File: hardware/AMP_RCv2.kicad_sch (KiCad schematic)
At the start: 46 parts, among them J1 USB_C_Receptacle_USB2.0_16P, SW1 SW_UP, SW2 SW_LEFT, SW3 SW_DOWN, SW4 SW_RIGHT, SW5 ON/OFF, U1 TPS61023, U2 MCP73831-2-OT, U3 JOYSTICK_LEFT, U4 JOYSTICK_RIGHT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

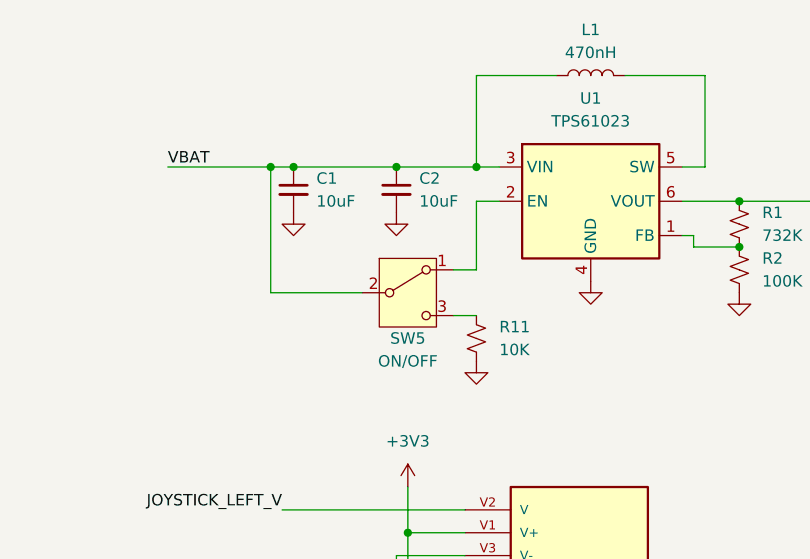
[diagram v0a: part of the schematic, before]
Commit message: Fix incorrect power switch wiring
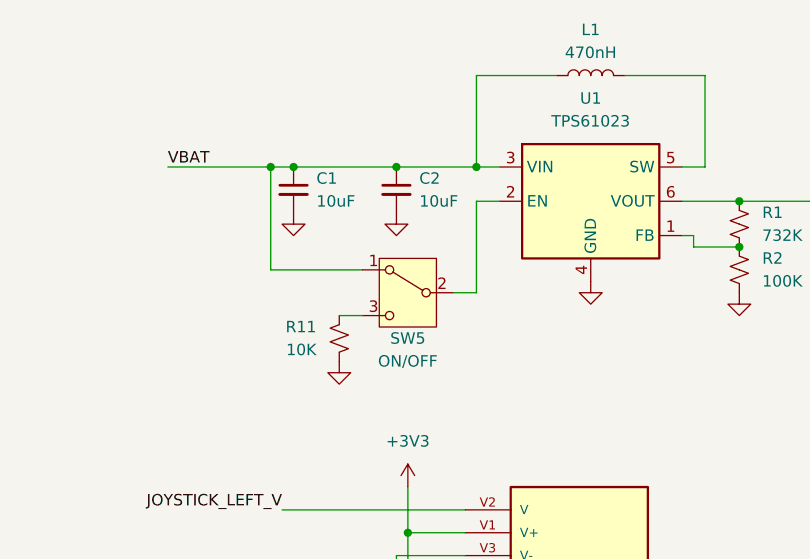
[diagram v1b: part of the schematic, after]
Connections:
- net VBAT: now also SW5.1 (A); no longer SW5.2 (B)
- net at U1.2 (EN): now also SW5.2 (B); no longer SW5.1 (A)
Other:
- moved on the sheet: R11
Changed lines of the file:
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@@
 	(wire
 		(pts
-			(xy 129.54 48.26) (xy 139.7 48.26)
+			(xy 226.06 87.63) (xy 233.68 87.63)
 		)
 		(stroke
@@
 	(wire
 		(pts
-			(xy 226.06 87.63) (xy 233.68 87.63)
+			(xy 143.51 87.63) (xy 143.51 95.25)
 		)
 		(stroke
@@
 	(wire
 		(pts
-			(xy 143.51 87.63) (xy 143.51 95.25)
+			(xy 219.71 129.54) (xy 232.41 129.54)
 		)
 		(stroke
@@
 	(wire
 		(pts
-			(xy 219.71 129.54) (xy 232.41 129.54)
+			(xy 40.64 132.08) (xy 40.64 137.16)
 		)
 		(stroke
@@
 	(wire
 		(pts
-			(xy 40.64 132.08) (xy 40.64 137.16)
+			(xy 175.26 41.91) (xy 176.53 41.91)
 		)
 		(stroke
@@
 	(wire
 		(pts
-			(xy 175.26 41.91) (xy 176.53 41.91)
+			(xy 149.86 48.26) (xy 152.4 48.26)
 		)
 		(stroke
@@
 	(wire
 		(pts
+			(xy 129.54 45.72) (xy 139.7 45.72)
+		)
+		(stroke
+			(width 0)
+			(type default)
+		)
+	)
+	(wire
+		(pts
 			(xy 78.74 68.58) (xy 99.06 68.58)
 		)
@@
 	(wire
 		(pts
-			(xy 149.86 50.8) (xy 152.4 50.8)
+			(xy 139.7 50.8) (xy 137.16 50.8)
 		)
 		(stroke
@@
 	(wire
 		(pts
-			(xy 152.4 38.1) (xy 152.4 45.72)
-		)
-		(stroke
-			(width 0)
-			(type default)
-		)
-	)
-	(wire
-		(pts
-			(xy 149.86 45.72) (xy 152.4 45.72)
+			(xy 152.4 38.1) (xy 152.4 48.26)
 		)
 		(stroke
@@
 	(wire
 		(pts
-			(xy 129.54 34.29) (xy 129.54 48.26)
+			(xy 129.54 34.29) (xy 129.54 45.72)
 		)
 		(stroke
@@
 		(lib_id "Switch:SW_SPDT")
 		(at 144.78 48.26 0)
+		(mirror y)
 		(unit 1)
 		(exclude_from_sim no)
@@
 	(symbol
 		(lib_id "Device:R_Small_US")
-		(at 152.4 53.34 0)
+		(at 137.16 53.34 0)
+		(mirror y)
 		(unit 1)
 		(exclude_from_sim no)
@@
 		(on_board yes)
 		(dnp no)
-		(fields_autoplaced yes)
 		(property "Reference" "R11"
-			(at 154.94 52.07 0)
+			(at 134.62 52.07 0)
 			(effects
 				(font
@@
 		)
 		(property "Value" "10K"
-			(at 154.94 54.61 0)
+			(at 134.62 54.61 0)
 			(effects
 				(font
@@
 		)
 		(property "Footprint" "Resistor_SMD:R_0805_2012Metric_Pad1.20x1.40mm_HandSolder"
-			(at 152.4 53.34 0)
+			(at 137.16 53.34 0)
 			(effects
 				(font
@@
 		)
 		(property "Datasheet" "~"
-			(at 152.4 53.34 0)
+			(at 137.16 53.34 0)
 			(effects
 				(font
@@
 		)
 		(property "Description" ""
-			(at 152.4 53.34 0)
+			(at 137.16 53.34 0)
 			(effects
 				(font
@@
 	(symbol
 		(lib_id "power:GND")
-		(at 152.4 55.88 0)
+		(at 137.16 55.88 0)
+		(mirror y)
 		(unit 1)
 		(exclude_from_sim no)
@@
 		(fields_autoplaced yes)
 		(property "Reference" "#PWR031"
-			(at 152.4 62.23 0)
+			(at 137.16 62.23 0)
 			(effects
 				(font
@@
 		)
 		(property "Value" "GND"
-			(at 152.4 60.96 0)
+			(at 137.16 60.96 0)
 			(effects
 				(font
@@
 		)
 		(property "Footprint" ""
-			(at 152.4 55.88 0)
+			(at 137.16 55.88 0)
 			(effects
 				(font
@@
 		)
 		(property "Datasheet" ""
-			(at 152.4 55.88 0)
+			(at 137.16 55.88 0)
 			(effects
 				(font
@@
 		)
 		(property "Description" ""
-			(at 152.4 55.88 0)
+			(at 137.16 55.88 0)
 			(effects
 				(font

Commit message: Replace USB-C port
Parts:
- J1: footprint Connector_USB:USB_C_Receptacle_GCT_USB4085 -> AMP_Custom:USB_C_Receptacle_Amphenol_C12402012
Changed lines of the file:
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@@
 			)
 		)
-		(property "Footprint" "Connector_USB:USB_C_Receptacle_GCT_USB4085"
+		(property "Footprint" "AMP_Custom:USB_C_Receptacle_Amphenol_C12402012"
 			(at 222.25 166.37 0)
 			(effects

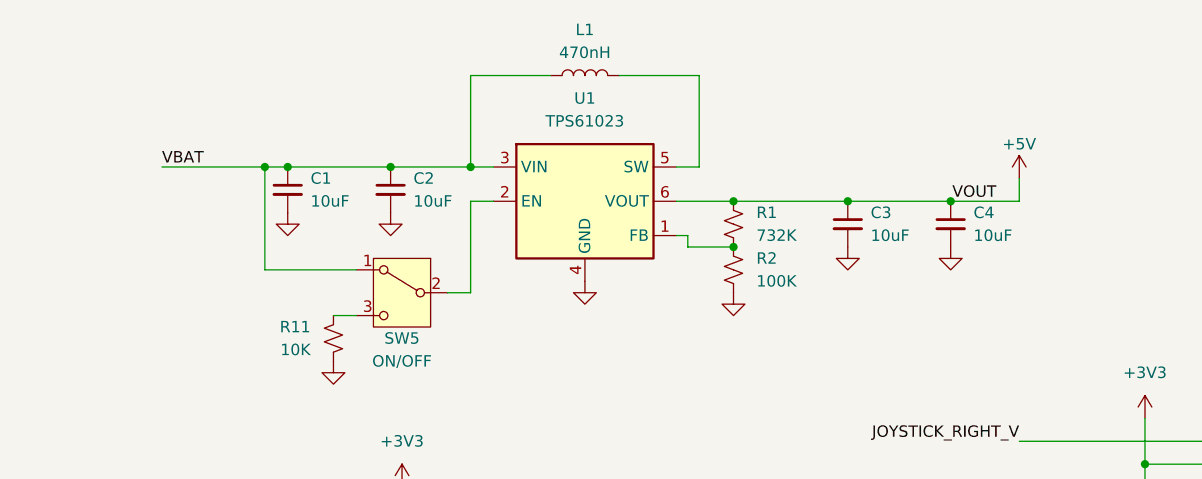
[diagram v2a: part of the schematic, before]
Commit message: Replace boost converter
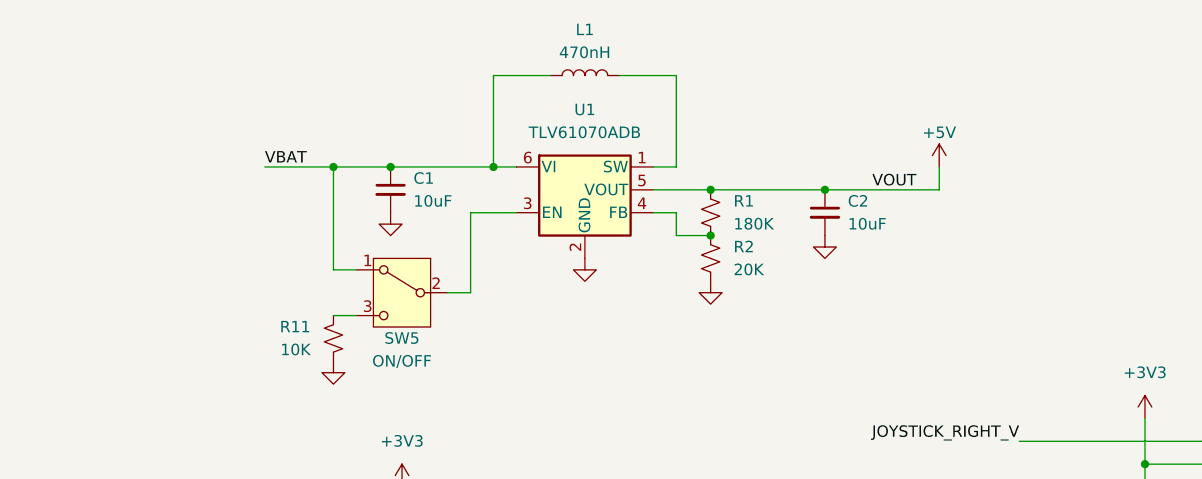
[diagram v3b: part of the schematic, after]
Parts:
- removed C1, C4: 10uF, Capacitor_SMD:C_0805_2012Metric_Pad1.18x1.45mm_HandSolder, symbol Device:C_Small
- removed U1: TPS61023, Package_TO_SOT_SMD:SOT-563, symbol AMP_Custom:TPS61023
- added U1: TLV61070ADB, Package_TO_SOT_SMD:SOT-23-6, symbol AMP_Custom:TLV61070ADB
- L1: footprint Inductor_SMD:L_Vishay_IHLP-1212 -> Inductor_SMD:L_Wuerth_MAPI-4030; DKPN (none) -> 74438357022
- R1: value 732K -> 180K
- R2: value 100K -> 20K
- renumbered C2 to C1, C3 to C2
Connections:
- net +5V: now also U1.5 (VOUT)
- net GND: now also U1.2 (GND)
- net VBAT: now also U1.6 (VI)
- net at SW5.2 (B): now also U1.3 (EN)
- net at R1.2, R2.1: now also U1.4 (FB)
- net at L1.2: now also U1.1 (SW)
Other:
- moved on the sheet: C2, R1, R2

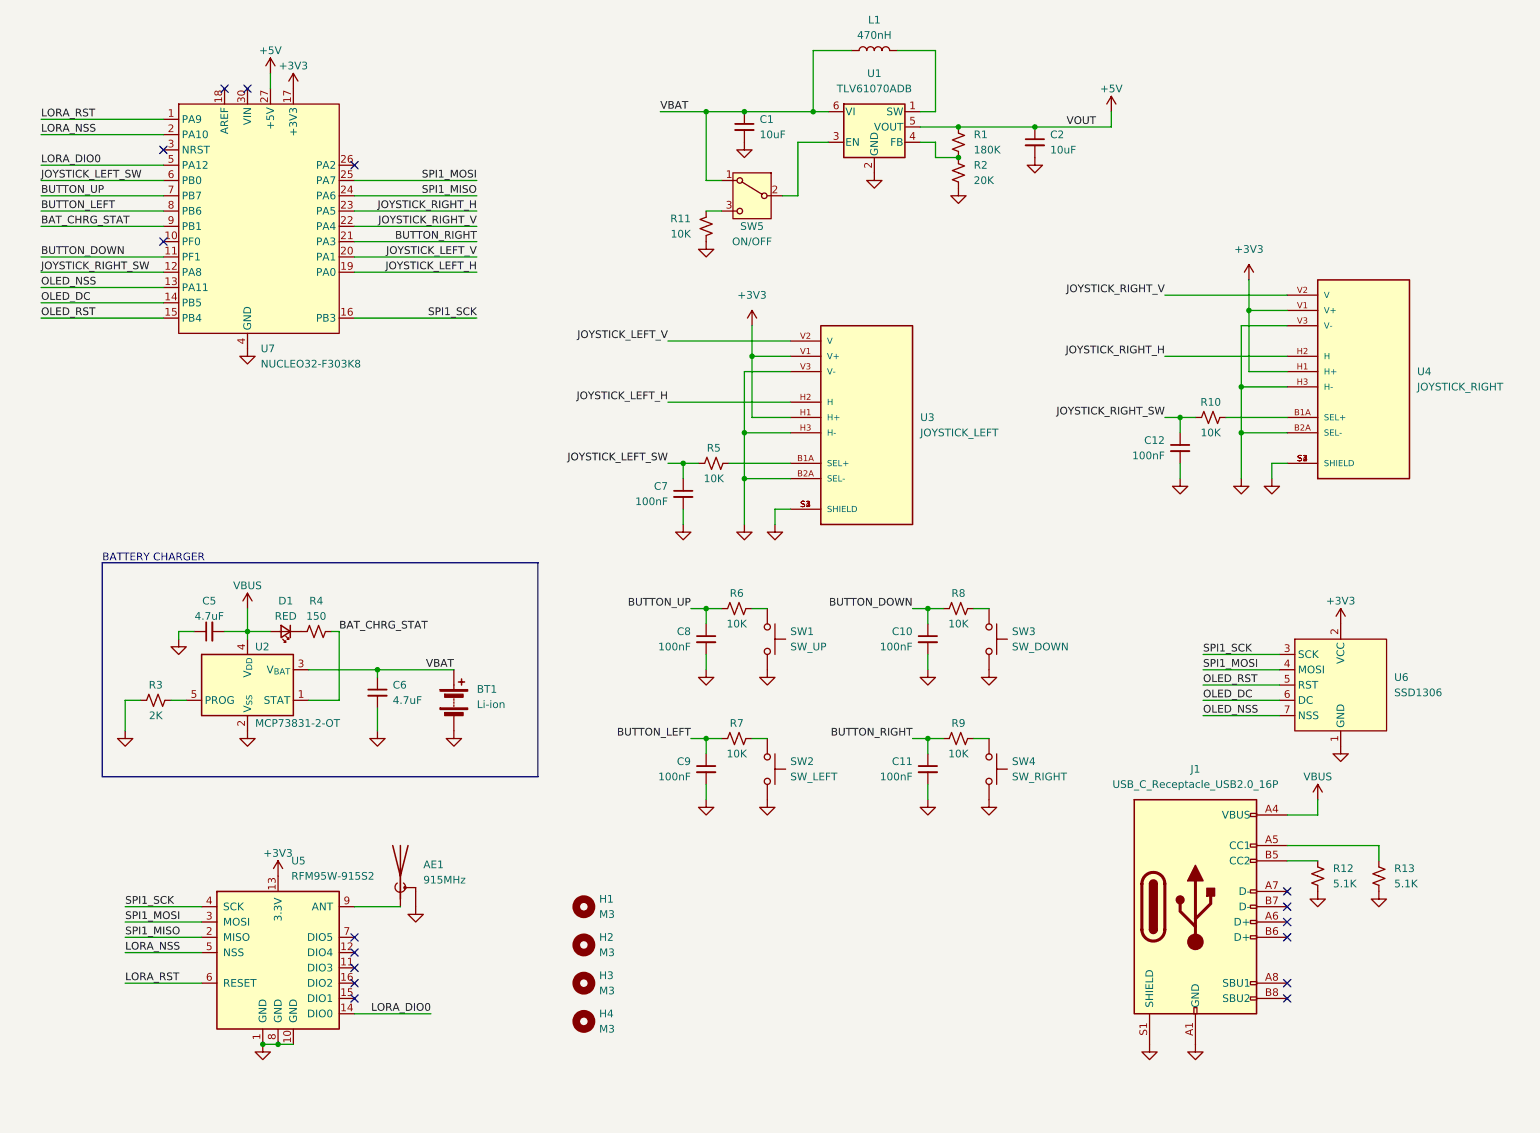
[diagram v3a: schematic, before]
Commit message: Clean up schematic and add optional second battery connector
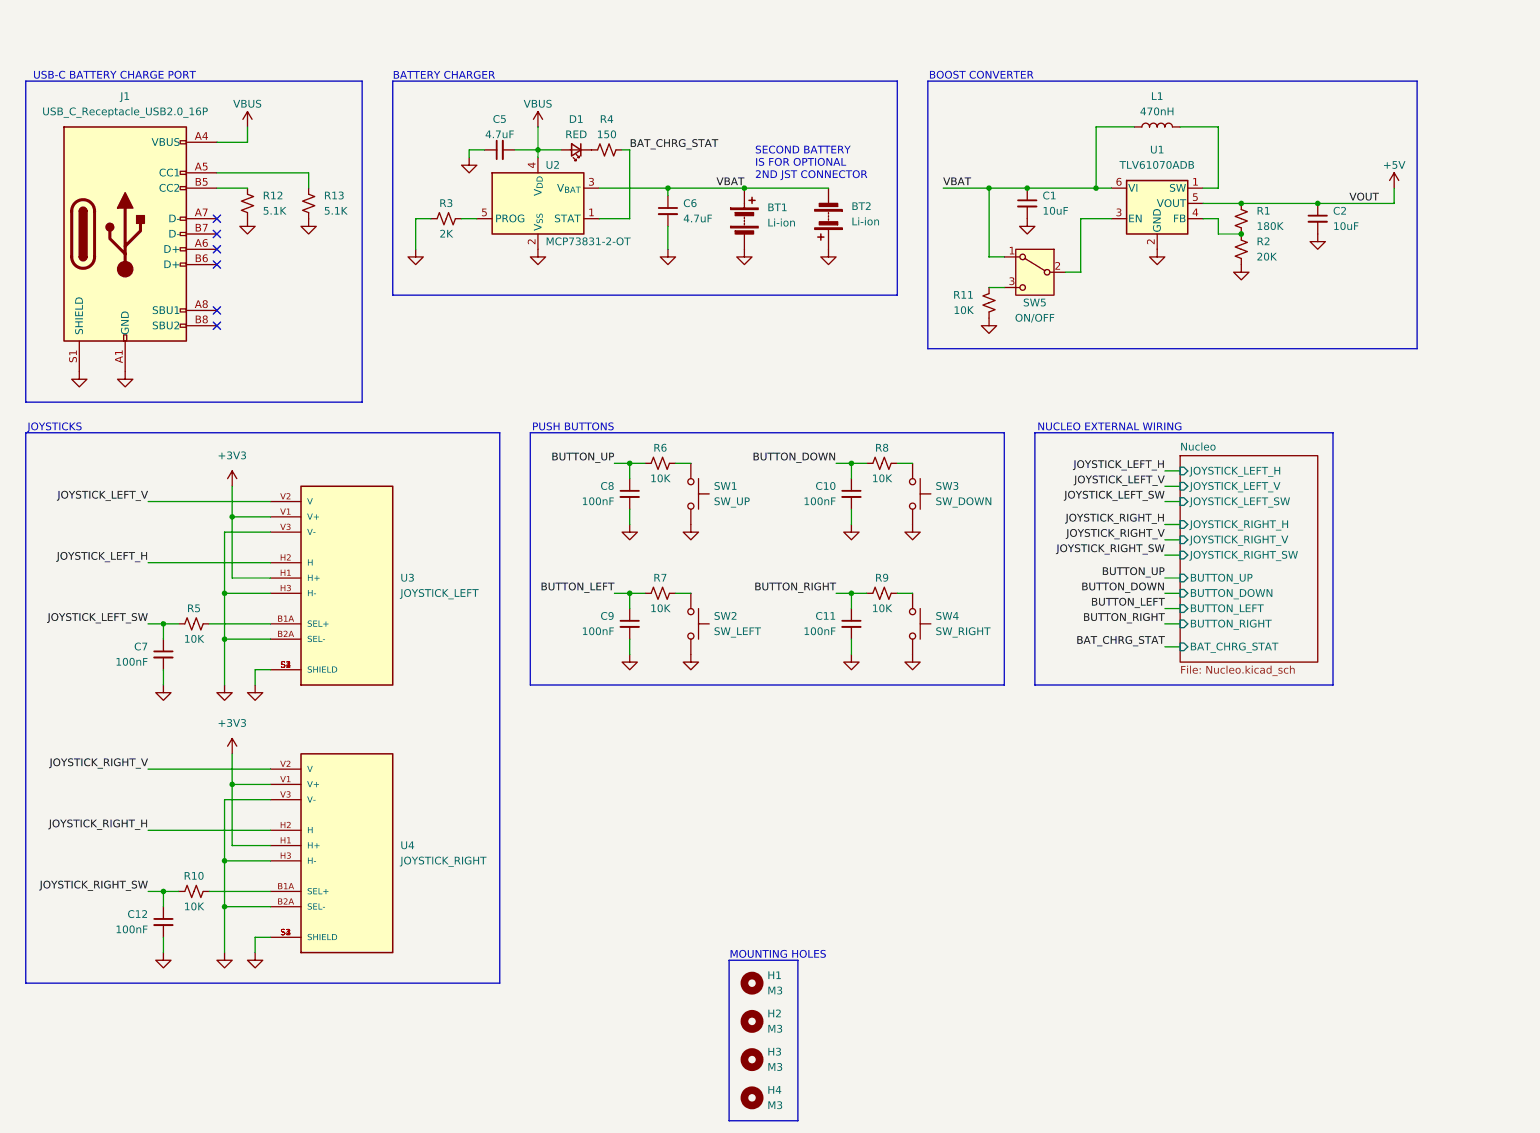
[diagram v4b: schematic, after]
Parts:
- removed AE1: 915MHz, Connector_Coaxial:SMA_Amphenol_132291_Vertical, symbol Device:Antenna_Shield
- removed U5: RFM95W-915S2, RF_Module:HOPERF_RFM9XW_SMD, symbol RF_Module:RFM95W-915S2
- removed U6: SSD1306, AMP_Custom:SSD1306_SPI, symbol AMP_Custom:SSD1306_SPI
- removed U7: NUCLEO32-F303K8, AMP_Custom:NUCLEO32, symbol AMP_Custom:NUCLEO32-F303K8
- added BT2: Li-ion, Connector_JST:JST_PH_B2B-PH-K_1x02_P2.00mm_Vertical, symbol Device:Battery
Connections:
- net GND: now also BT2.1 (+)
- net VBAT: now also BT2.2 (-)
- no-connect marks 16 -> 6
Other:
- added sheet Nucleo (Nucleo.kicad_sch)
- note added: "BOOST CONVERTER"
- note added: "JOYSTICKS"
- note added: "MOUNTING HOLES"
- note added: "NUCLEO EXTERNAL WIRING"
- note added: "PUSH BUTTONS"
- note added: "SECOND BATTERY IS FOR OPTIONAL 2ND JST CONNECTOR"
- note added: "USB-C BATTERY CHARGE PORT"
- moved on the sheet: BT1, C1, C10, C11, C12, C2, C5, C6, C7, C8, C9, D1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

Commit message: Finishing touches
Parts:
- J1: footprint AMP_Custom:USB_C_Receptacle_Amphenol_C12402012 -> Connector_USB:USB_C_Receptacle_GCT_USB4085
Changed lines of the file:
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@@
 		(title "AMP_RCv2")
 		(date "2024-03-14")
-		(rev "A")
+		(rev "B")
 		(company "Autonomous Motorsports Purdue")
 	)
@@
 			)
 		)
-		(property "Footprint" "AMP_Custom:USB_C_Receptacle_Amphenol_C12402012"
+		(property "Footprint" "Connector_USB:USB_C_Receptacle_GCT_USB4085"
 			(at 44.45 54.61 0)
 			(effects
